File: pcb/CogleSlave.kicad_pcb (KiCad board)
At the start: 2 copper layers, 24.9 x 20.8 mm, 7 parts, among them P1 CONN_01X04, P2 CONN_01X04, P3 CONN_01X08, U1 PCF8591T

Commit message: 基板レイアウトを修正 1.2
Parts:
- moved P1 0.51 mm to (176.8, 118.7)
- moved P2 0.51 mm to (189.5, 118.7)
- moved C1 0.38 mm to (180.0, 114.6)
- moved U1 0.25 mm to (187.7, 111.0)
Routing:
- net /AIN1: track 20.0 -> 29.1 mm
- net /AIN2: track 17.5 -> 25.5 mm
- net /AIN0: track 22.5 -> 30.5 mm
- net /AIN3: track 15.0 -> 21.9 mm
- net GND: track 2.90 -> 7.97 mm
- net /A1: track 11.4 -> 13.8 mm, vias 2 -> 0
- net +5V: track 42.9 -> 45.0 mm
- net /SDA: track 18.6 -> 20.6 mm
- net /SCL: track 15.8 -> 17.8 mm
- net /A0: track 10.4 -> 12.0 mm
- net /A2: track 14.8 -> 16.3 mm, vias 2 -> 0
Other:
- board size 24.9 x 20.8 mm -> 24.9 x 22.6 mm
- net class Default: via_dia 1.2 -> 1.5
- rule via_min_size: 1.2 -> 1.3

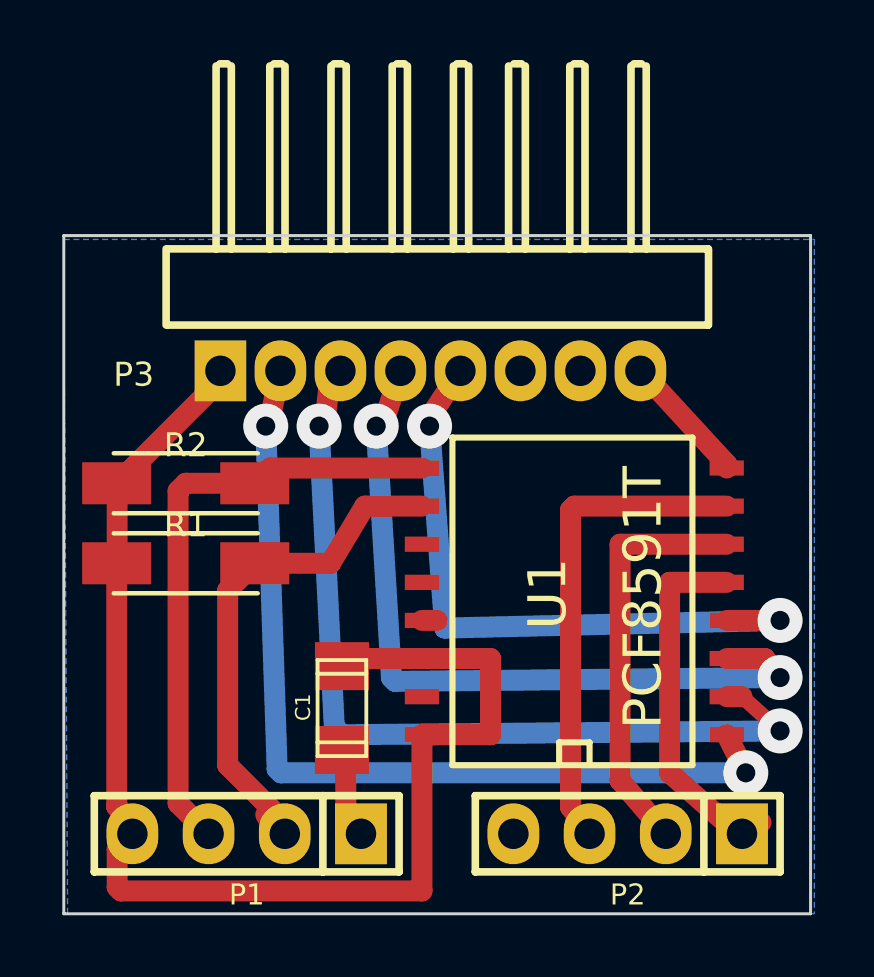
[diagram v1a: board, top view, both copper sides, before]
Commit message: Arduino向けライブラリv1.0を追加
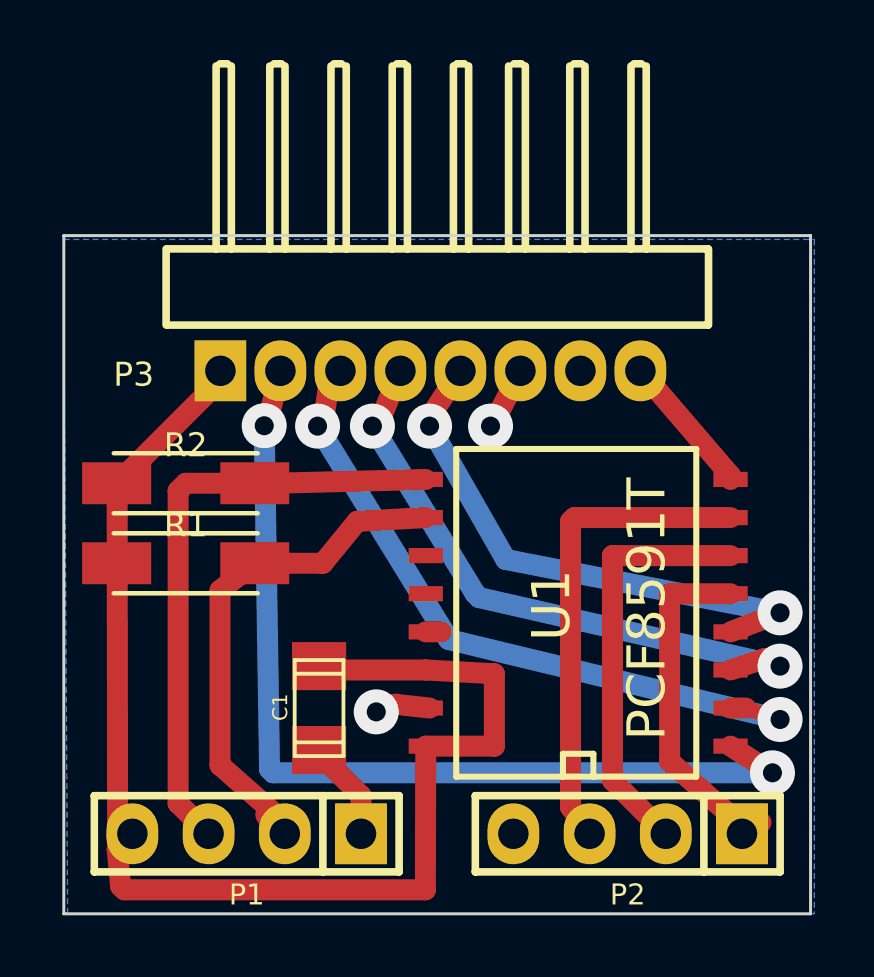
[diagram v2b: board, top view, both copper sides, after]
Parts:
- moved C1 0.76 mm to (179.2, 114.6)
- moved U1 0.40 mm to (187.8, 111.4)
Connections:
- P3 pad 6: (no net) -> /AOUT
- U1 pad 15: (no net) -> /AOUT
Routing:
- net /AIN1: track 29.1 -> 23.3 mm
- net /AIN2: track 25.5 -> 20.9 mm
- net /AOUT: track 0.00 -> 4.24 mm, vias 0 -> 2
- net /AIN3: track 21.9 -> 18.4 mm
- net /AIN0: track 30.5 -> 31.8 mm
- net +5V: track 45.0 -> 46.2 mm
- net GND: track 7.97 -> 8.77 mm
- net /A0: track 12.0 -> 11.3 mm
